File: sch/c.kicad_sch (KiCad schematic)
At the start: 1 part

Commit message: Update
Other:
- moved on the sheet: J?
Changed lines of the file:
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@@
 (kicad_sch (version 20211123) (generator eeschema)
   (paper "A4")
-  (symbol (lib_id "Connector:XLR3") (at 157.48 95.25 0) (unit 1)
+  (symbol (lib_id "Connector:XLR3") (at 140.97 93.98 0) (unit 1)
     (in_bom yes) (on_board yes) (fields_autoplaced)
-    (property "Reference" "J?" (id 0) (at 157.48 85.09 0))
-    (property "Value" "XLR3" (id 1) (at 157.48 87.63 0))
-    (property "Footprint" "" (id 2) (at 157.48 95.25 0)
+    (property "Reference" "J?" (id 0) (at 140.97 83.82 0))
+    (property "Value" "XLR3" (id 1) (at 140.97 86.36 0))
+    (property "Footprint" "" (id 2) (at 140.97 93.98 0)
       (effects (font (size 1.27 1.27)) hide)
     )
-    (property "Datasheet" " ~" (id 3) (at 157.48 95.25 0)
+    (property "Datasheet" " ~" (id 3) (at 140.97 93.98 0)
       (effects (font (size 1.27 1.27)) hide)
     )
@@
     (pin "3")
   )
-  (sheet (at 179.07 90.17) (size 27.94 11.43) (fields_autoplaced)
+  (sheet (at 153.67 88.9) (size 27.94 11.43) (fields_autoplaced)
     (stroke (width 0.1524) (type solid) (color 0 0 0 0))
     (fill (color 0 0 0 0.0000))
-    (property "Sheet name" "D" (id 0) (at 179.07 89.4584 0)
+    (property "Sheet name" "D" (id 0) (at 153.67 88.1884 0)
       (effects (font (size 1.27 1.27)) (justify left bottom))
     )
-    (property "Sheet file" "d.kicad_sch" (id 1) (at 179.07 102.1846 0)
+    (property "Sheet file" "d.kicad_sch" (id 1) (at 153.67 100.9146 0)
       (effects (font (size 1.27 1.27)) (justify left top))
     )

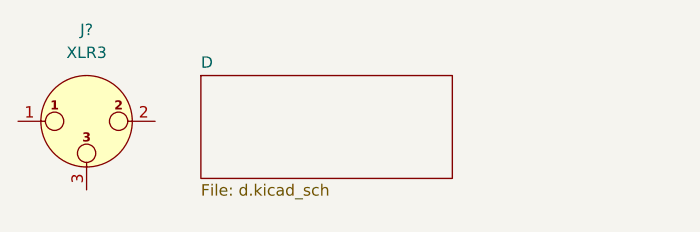
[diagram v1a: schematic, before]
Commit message: Add file and sheet instance with spaces. Anotate parts.
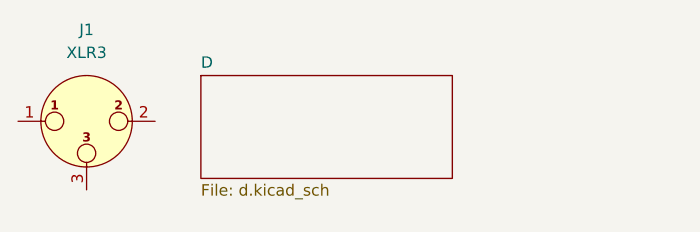
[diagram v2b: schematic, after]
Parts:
- gave numbers to parts that had none: 1
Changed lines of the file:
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@@
   (symbol (lib_id "Connector:XLR3") (at 140.97 93.98 0) (unit 1)
     (in_bom yes) (on_board yes) (fields_autoplaced)
-    (property "Reference" "J?" (id 0) (at 140.97 83.82 0))
+    (property "Reference" "J1" (id 0) (at 140.97 83.82 0))
     (property "Value" "XLR3" (id 1) (at 140.97 86.36 0))
     (property "Footprint" "" (id 2) (at 140.97 93.98 0)
